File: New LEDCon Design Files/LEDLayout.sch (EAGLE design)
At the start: 7 parts

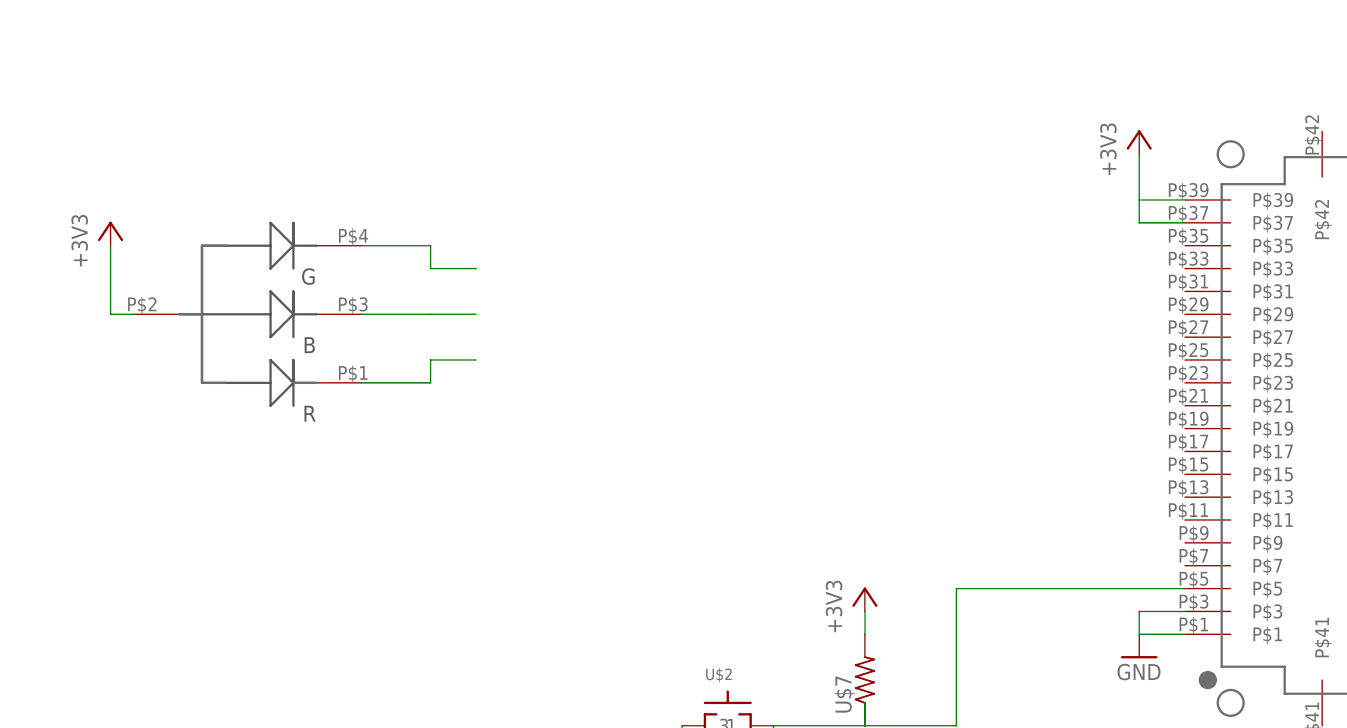
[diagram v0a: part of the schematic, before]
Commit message: Finished routing 1st prototype
Added WS2801, choice resistors & finished routing
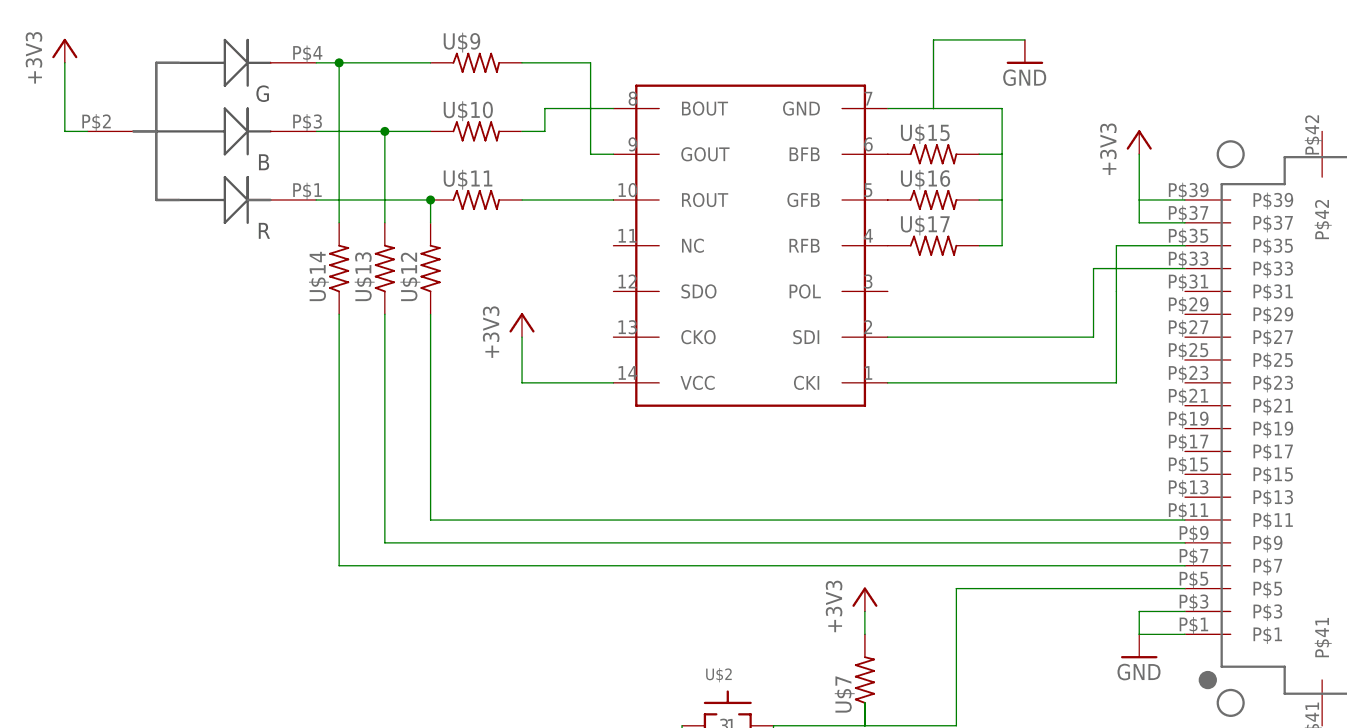
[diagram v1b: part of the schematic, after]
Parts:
- added U$10, U$11, U$12, U$13, U$14, U$15, U$16, U$17, U$9: (no value), GW-devices:RF-R0805
- added U$8: WS2801, GW-devices:WS2801
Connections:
- new net N$10: U$4.P$33, U$8.SDI
- new net N$11: U$15.1, U$8.BFB
- new net N$12: U$16.1, U$8.GFB
- new net N$13: U$17.1, U$8.RFB
- new net N$14: U$4.P$35, U$8.CKI
- new net N$15: U$14.1, U$4.P$7
- new net N$16: U$13.1, U$4.P$9
- new net N$17: U$12.1, U$4.P$11
- new net N$7: U$11.1, U$12.2, U$5.RED
- new net N$8: U$10.2, U$8.BOUT
- new net N$9: U$8.GOUT, U$9.2
- net +3V3: now also U$8.VCC
- net GND: now also U$15.2, U$16.2, U$17.2, U$8.GND
- net N$4: now also U$14.2, U$9.1
- net N$5: now also U$10.1, U$13.2
- net N$6: now also U$11.2, U$8.ROUT; no longer U$5.RED
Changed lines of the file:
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@@
 <part name="+3V3" library="supply1" deviceset="+3V3" device=""/>
 <part name="+3V5" library="supply1" deviceset="+3V3" device=""/>
+<part name="U$8" library="GW-devices" deviceset="WS2801" device=""/>
+<part name="U$9" library="GW-devices" deviceset="RF-R" device="0805"/>
+<part name="U$10" library="GW-devices" deviceset="RF-R" device="0805"/>
+<part name="U$11" library="GW-devices" deviceset="RF-R" device="0805"/>
+<part name="U$12" library="GW-devices" deviceset="RF-R" device="0805"/>
+<part name="U$13" library="GW-devices" deviceset="RF-R" device="0805"/>
+<part name="U$14" library="GW-devices" deviceset="RF-R" device="0805"/>
+<part name="GND7" library="supply1" deviceset="GND" device=""/>
+<part name="+3V6" library="supply1" deviceset="+3V3" device=""/>
+<part name="U$15" library="GW-devices" deviceset="RF-R" device="0805"/>
+<part name="U$16" library="GW-devices" deviceset="RF-R" device="0805"/>
+<part name="U$17" library="GW-devices" deviceset="RF-R" device="0805"/>
 </parts>
 <sheets>
@@
 <instance part="U$3" gate="G$1" x="58.42" y="10.16" rot="R180"/>
 <instance part="U$4" gate="G$1" x="10.16" y="-17.78"/>
-<instance part="U$5" gate="G$1" x="-111.76" y="-5.08" rot="R180">
-<attribute name="MFGN" x="-111.76" y="-5.08" size="1.778" layer="96" rot="R180" display="off"/>
-<attribute name="MFGP" x="-111.76" y="-5.08" size="1.778" layer="96" rot="R180" display="off"/>
+<instance part="U$5" gate="G$1" x="-116.84" y="15.24" rot="R180">
+<attribute name="MFGN" x="-116.84" y="15.24" size="1.778" layer="96" rot="R180" display="off"/>
+<attribute name="MFGP" x="-116.84" y="15.24" size="1.778" layer="96" rot="R180" display="off"/>
 </instance>
 <instance part="GND1" gate="1" x="27.94" y="-43.18"/>
@@
 <instance part="U$7" gate="G$1" x="-40.64" y="-45.72" rot="R90"/>
 <instance part="+3V3" gate="G$1" x="-40.64" y="-35.56"/>
-<instance part="+3V5" gate="G$1" x="-124.46" y="5.08"/>
+<instance part="+3V5" gate="G$1" x="-129.54" y="25.4"/>
+<instance part="U$8" gate="G$1" x="-55.88" y="2.54" rot="R180"/>
+<instance part="U$9" gate="G$1" x="-83.82" y="22.86"/>
+<instance part="U$10" gate="G$1" x="-83.82" y="15.24"/>
+<instance part="U$11" gate="G$1" x="-83.82" y="7.62"/>
+<instance part="U$12" gate="G$1" x="-88.9" y="0" rot="R90"/>
+<instance part="U$13" gate="G$1" x="-93.98" y="0" rot="R90"/>
+<instance part="U$14" gate="G$1" x="-99.06" y="0" rot="R90"/>
+<instance part="GND7" gate="1" x="-22.86" y="22.86"/>
+<instance part="+3V6" gate="G$1" x="-78.74" y="-5.08"/>
+<instance part="U$15" gate="G$1" x="-33.02" y="12.7"/>
+<instance part="U$16" gate="G$1" x="-33.02" y="7.62"/>
+<instance part="U$17" gate="G$1" x="-33.02" y="2.54"/>
 </instances>
 <busses>
@@
 <wire x1="-60.96" y1="-53.34" x2="-66.04" y2="-53.34" width="0.1524" layer="91"/>
 </segment>
+<segment>
+<pinref part="U$8" gate="G$1" pin="GND"/>
+<wire x1="-38.1" y1="17.78" x2="-33.02" y2="17.78" width="0.1524" layer="91"/>
+<wire x1="-33.02" y1="17.78" x2="-33.02" y2="25.4" width="0.1524" layer="91"/>
+<pinref part="GND7" gate="1" pin="GND"/>
+<wire x1="-33.02" y1="25.4" x2="-22.86" y2="25.4" width="0.1524" layer="91"/>
+<pinref part="U$17" gate="G$1" pin="2"/>
+<wire x1="-27.94" y1="2.54" x2="-25.4" y2="2.54" width="0.1524" layer="91"/>
+<wire x1="-25.4" y1="2.54" x2="-25.4" y2="7.62" width="0.1524" layer="91"/>
+<pinref part="U$16" gate="G$1" pin="2"/>
+<wire x1="-25.4" y1="7.62" x2="-27.94" y2="7.62" width="0.1524" layer="91"/>
+<pinref part="U$15" gate="G$1" pin="2"/>
+<wire x1="-27.94" y1="12.7" x2="-25.4" y2="12.7" width="0.1524" layer="91"/>
+<wire x1="-25.4" y1="12.7" x2="-25.4" y2="7.62" width="0.1524" layer="91"/>
+<wire x1="-25.4" y1="12.7" x2="-25.4" y2="17.78" width="0.1524" layer="91"/>
+<wire x1="-25.4" y1="17.78" x2="-33.02" y2="17.78" width="0.1524" layer="91"/>
+</segment>
 </net>
 <net name="+3V3" class="0">
@@
 <segment>
 <pinref part="U$5" gate="G$1" pin="ANODE"/>
-<wire x1="-121.92" y1="-5.08" x2="-124.46" y2="-5.08" width="0.1524" layer="91"/>
+<wire x1="-127" y1="15.24" x2="-129.54" y2="15.24" width="0.1524" layer="91"/>
 <pinref part="+3V5" gate="G$1" pin="+3V3"/>
-<wire x1="-124.46" y1="-5.08" x2="-124.46" y2="2.54" width="0.1524" layer="91"/>
+<wire x1="-129.54" y1="15.24" x2="-129.54" y2="22.86" width="0.1524" layer="91"/>
+</segment>
+<segment>
+<pinref part="U$8" gate="G$1" pin="VCC"/>
+<pinref part="+3V6" gate="G$1" pin="+3V3"/>
+<wire x1="-68.58" y1="-12.7" x2="-78.74" y2="-12.7" width="0.1524" layer="91"/>
+<wire x1="-78.74" y1="-12.7" x2="-78.74" y2="-7.62" width="0.1524" layer="91"/>
 </segment>
 </net>
@@
 <segment>
 <pinref part="U$5" gate="G$1" pin="GREEN"/>
-<wire x1="-96.52" y1="2.54" x2="-88.9" y2="2.54" width="0.1524" layer="91"/>
-<wire x1="-83.82" y1="0" x2="-88.9" y2="0" width="0.1524" layer="91"/>
-<wire x1="-88.9" y1="0" x2="-88.9" y2="2.54" width="0.1524" layer="91"/>
+<wire x1="-101.6" y1="22.86" x2="-99.06" y2="22.86" width="0.1524" layer="91"/>
+<pinref part="U$9" gate="G$1" pin="1"/>
+<pinref part="U$14" gate="G$1" pin="2"/>
+<wire x1="-99.06" y1="22.86" x2="-88.9" y2="22.86" width="0.1524" layer="91"/>
+<wire x1="-99.06" y1="5.08" x2="-99.06" y2="22.86" width="0.1524" layer="91"/>
+<junction x="-99.06" y="22.86"/>
 </segment>
 </net>
@@
 <segment>
 <pinref part="U$5" gate="G$1" pin="BLUE"/>
-<wire x1="-96.52" y1="-5.08" x2="-88.9" y2="-5.08" width="0.1524" layer="91"/>
-<wire x1="-83.82" y1="-5.08" x2="-88.9" y2="-5.08" width="0.1524" layer="91"/>
+<wire x1="-101.6" y1="15.24" x2="-93.98" y2="15.24" width="0.1524" layer="91"/>
+<pinref part="U$10" gate="G$1" pin="1"/>
+<pinref part="U$13" gate="G$1" pin="2"/>
+<wire x1="-93.98" y1="15.24" x2="-88.9" y2="15.24" width="0.1524" layer="91"/>
+<wire x1="-93.98" y1="5.08" x2="-93.98" y2="15.24" width="0.1524" layer="91"/>
+<junction x="-93.98" y="15.24"/>
+</segment>
+</net>
+<net name="N$7" class="0">
+<segment>
+<pinref part="U$11" gate="G$1" pin="1"/>
+<pinref part="U$12" gate="G$1" pin="2"/>
+<wire x1="-88.9" y1="5.08" x2="-88.9" y2="7.62" width="0.1524" layer="91"/>
+<pinref part="U$5" gate="G$1" pin="RED"/>
+<wire x1="-101.6" y1="7.62" x2="-88.9" y2="7.62" width="0.1524" layer="91"/>
+<junction x="-88.9" y="7.62"/>
 </segment>
 </net>
 <net name="N$6" class="0">
 <segment>
-<pinref part="U$5" gate="G$1" pin="RED"/>
-<wire x1="-96.52" y1="-12.7" x2="-88.9" y2="-12.7" width="0.1524" layer="91"/>
-<wire x1="-83.82" y1="-10.16" x2="-88.9" y2="-10.16" width="0.1524" layer="91"/>
-<wire x1="-88.9" y1="-10.16" x2="-88.9" y2="-12.7" width="0.1524" layer="91"/>
-</segment>
-</net>
+<pinref part="U$11" gate="G$1" pin="2"/>
+<pinref part="U$8" gate="G$1" pin="ROUT"/>
+<wire x1="-78.74" y1="7.62" x2="-68.58" y2="7.62" width="0.1524" layer="91"/>
+</segment>
+</net>
+<net name="N$8" class="0">
+<segment>
+<pinref part="U$10" gate="G$1" pin="2"/>
+<wire x1="-78.74" y1="15.24" x2="-76.2" y2="15.24" width="0.1524" layer="91"/>
+<wire x1="-76.2" y1="15.24" x2="-76.2" y2="17.78" width="0.1524" layer="91"/>
+<pinref part="U$8" gate="G$1" pin="BOUT"/>
+<wire x1="-76.2" y1="17.78" x2="-68.58" y2="17.78" width="0.1524" layer="91"/>
+</segment>
+</net>
+<net name="N$9" class="0">
+<segment>
+<pinref part="U$9" gate="G$1" pin="2"/>
+<wire x1="-78.74" y1="22.86" x2="-71.12" y2="22.86" width="0.1524" layer="91"/>
+<wire x1="-71.12" y1="22.86" x2="-71.12" y2="12.7" width="0.1524" layer="91"/>
+<pinref part="U$8" gate="G$1" pin="GOUT"/>
+<wire x1="-71.12" y1="12.7" x2="-68.58" y2="12.7" width="0.1524" layer="91"/>
+</segment>
+</net>
+<net name="N$11" class="0">
+<segment>
+<pinref part="U$8" gate="G$1" pin="BFB"/>
+<pinref part="U$15" gate="G$1" pin="1"/>
+</segment>
+</net>
+<net name="N$12" class="0">
+<segment>
+<pinref part="U$8" gate="G$1" pin="GFB"/>
+<pinref part="U$16" gate="G$1" pin="1"/>
+</segment>
+</net>
+<net name="N$13" class="0">
+<segment>
+<pinref part="U$8" gate="G$1" pin="RFB"/>
+<pinref part="U$17" gate="G$1" pin="1"/>
+</segment>
+</net>
+<net name="N$10" class="0">
+<segment>
+<pinref part="U$8" gate="G$1" pin="SDI"/>
+<wire x1="-38.1" y1="-7.62" x2="-15.24" y2="-7.62" width="0.1524" layer="91"/>
+<wire x1="-15.24" y1="-7.62" x2="-15.24" y2="0" width="0.1524" layer="91"/>
+<pinref part="U$4" gate="G$1" pin="P$33"/>
+<wire x1="-5.08" y1="0" x2="-15.24" y2="0" width="0.1524" layer="91"/>
+</segment>
+</net>
+<net name="N$14" class="0">
+<segment>
+<wire x1="-12.7" y1="-2.54" x2="-12.7" y2="-12.7" width="0.1524" layer="91"/>
+<pinref part="U$8" gate="G$1" pin="CKI"/>
+<wire x1="-12.7" y1="-12.7" x2="-38.1" y2="-12.7" width="0.1524" layer="91"/>
+<wire x1="-12.7" y1="-2.54" x2="-12.7" y2="2.54" width="0.1524" layer="91"/>
+<pinref part="U$4" gate="G$1" pin="P$35"/>
+<wire x1="-12.7" y1="2.54" x2="-5.08" y2="2.54" width="0.1524" layer="91"/>
+</segment>
+</net>
+<net name="N$15" class="0">
+<segment>
+<pinref part="U$4" gate="G$1" pin="P$7"/>
+<pinref part="U$14" gate="G$1" pin="1"/>
+<wire x1="-5.08" y1="-33.02" x2="-99.06" y2="-33.02" width="0.1524" layer="91"/>
+<wire x1="-99.06" y1="-33.02" x2="-99.06" y2="-5.08" width="0.1524" layer="91"/>
+</segment>
+</net>
+<net name="N$16" class="0">
+<segment>
+<pinref part="U$13" gate="G$1" pin="1"/>
+<wire x1="-93.98" y1="-5.08" x2="-93.98" y2="-30.48" width="0.1524" layer="91"/>
+<pinref part="U$4" gate="G$1" pin="P$9"/>
+<wire x1="-93.98" y1="-30.48" x2="-5.08" y2="-30.48" width="0.1524" layer="91"/>
+</segment>
+</net>
+<net name="N$17" class="0">
+<segment>
+<pinref part="U$4" gate="G$1" pin="P$11"/>
+<pinref part="U$12" gate="G$1" pin="1"/>
+<wire x1="-5.08" y1="-27.94" x2="-88.9" y2="-27.94" width="0.1524" layer="91"/>
+<wire x1="-88.9" y1="-27.94" x2="-88.9" y2="-5.08" width="0.1524" layer="91"/>
+</segment>
+</net>

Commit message: Added JTAG header, fixed data / clock switch
Moved TXB0104 to front side
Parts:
- removed U$12, U$13, U$14: (no value), GW-devices:RF-R0805
- added U$18: (no value), GW-devices:RF-R0805
- added U$19: 2X10JTAG, KW2:2X10JTAG
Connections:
- removed net N$15: U$14.1, U$4.P$7
- removed net N$16: U$13.1, U$4.P$9
- removed net N$17: U$12.1, U$4.P$11
- new net N$18: U$19.P$4, U$4.P$8
- new net N$19: U$4.P$14
- new net N$20: U$19.P$8, U$4.P$10
- new net N$21: U$19.P$10, U$4.P$6
- new net N$22: U$4.P$12
- net +3V3: now also U$18.1, U$19.P$1
- net CLK_5V: now also U$1.P$3, U$18.2, U$6.P$12; no longer U$1.P$2, U$6.P$13
- net DAT_5V: now also U$1.P$2, U$6.P$13; no longer U$1.P$3, U$6.P$12
- net GND: now also U$19.P$15, U$19.P$17, U$19.P$19, U$19.P$3, U$19.P$5, U$19.P$9
- net N$1: now also U$4.P$26; no longer U$4.P$24
- net N$2: now also U$4.P$24; no longer U$4.P$26
- net N$4: no longer U$14.2
- net N$5: no longer U$13.2
- net N$7: no longer U$12.2
